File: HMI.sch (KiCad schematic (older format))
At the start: 34 parts, among them J24 Display, J25 SPI Interface, J26 I2C Interface, J27 LED3, J28 LED4, J29 Key 3, J30 Key 4, J31 Key 1, J32 Key 2, Q8 BC817, Q9 BC817, U9 74HC245

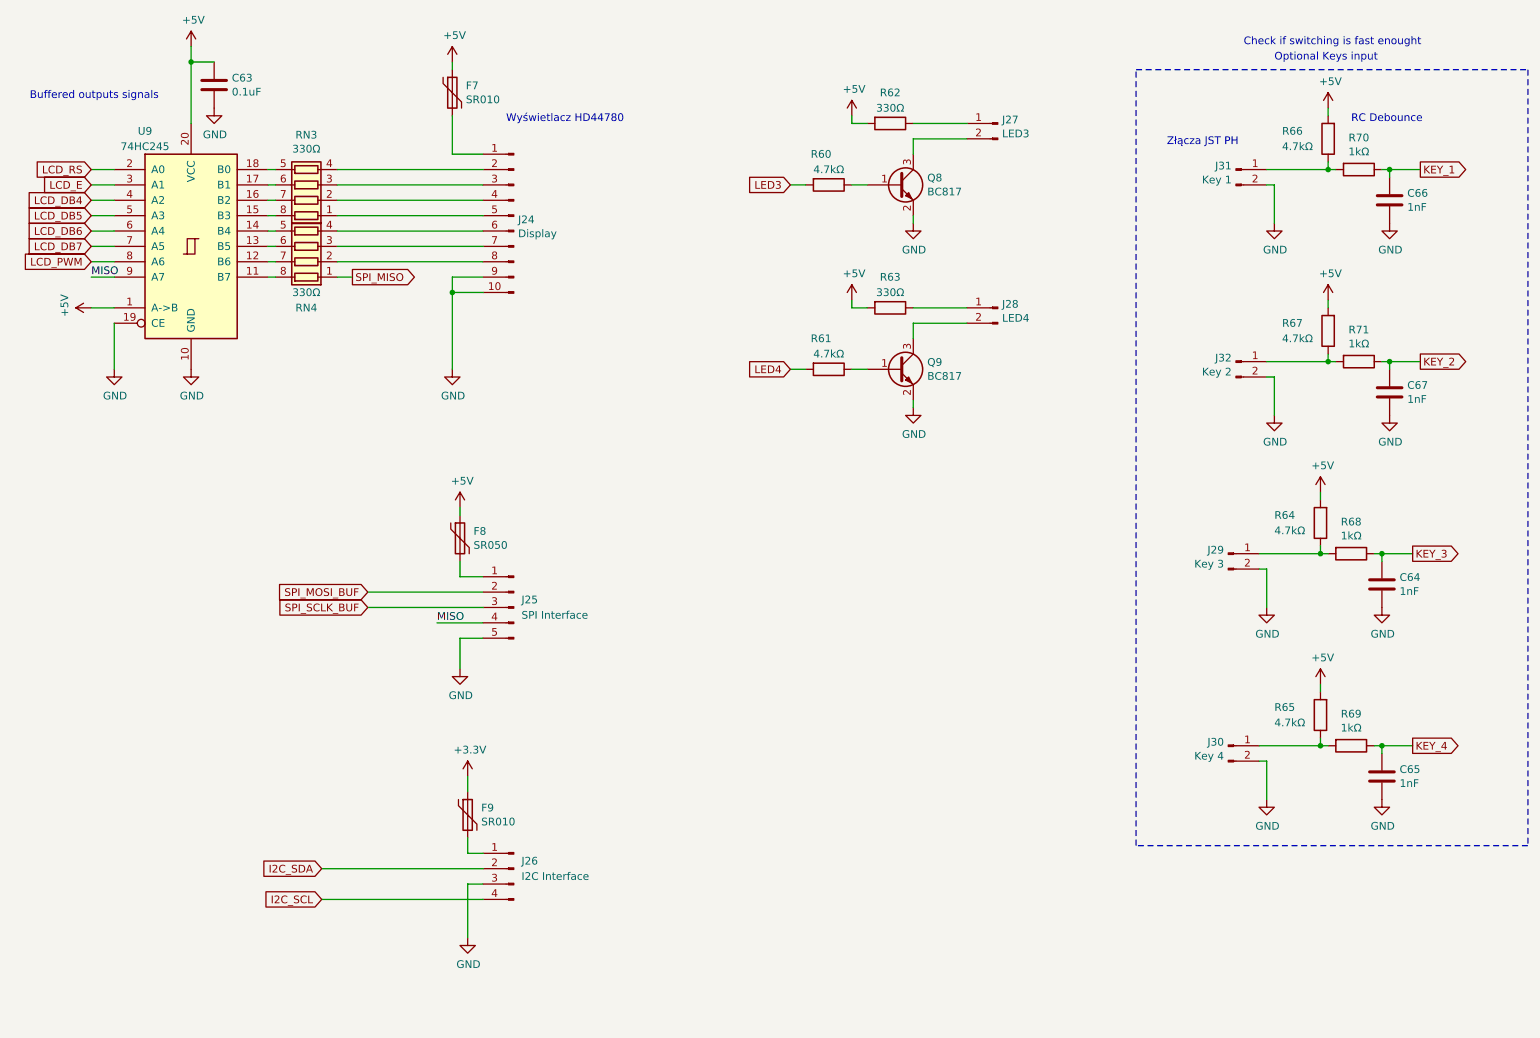
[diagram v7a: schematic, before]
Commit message: Improve Emergency, Added TVS diodes
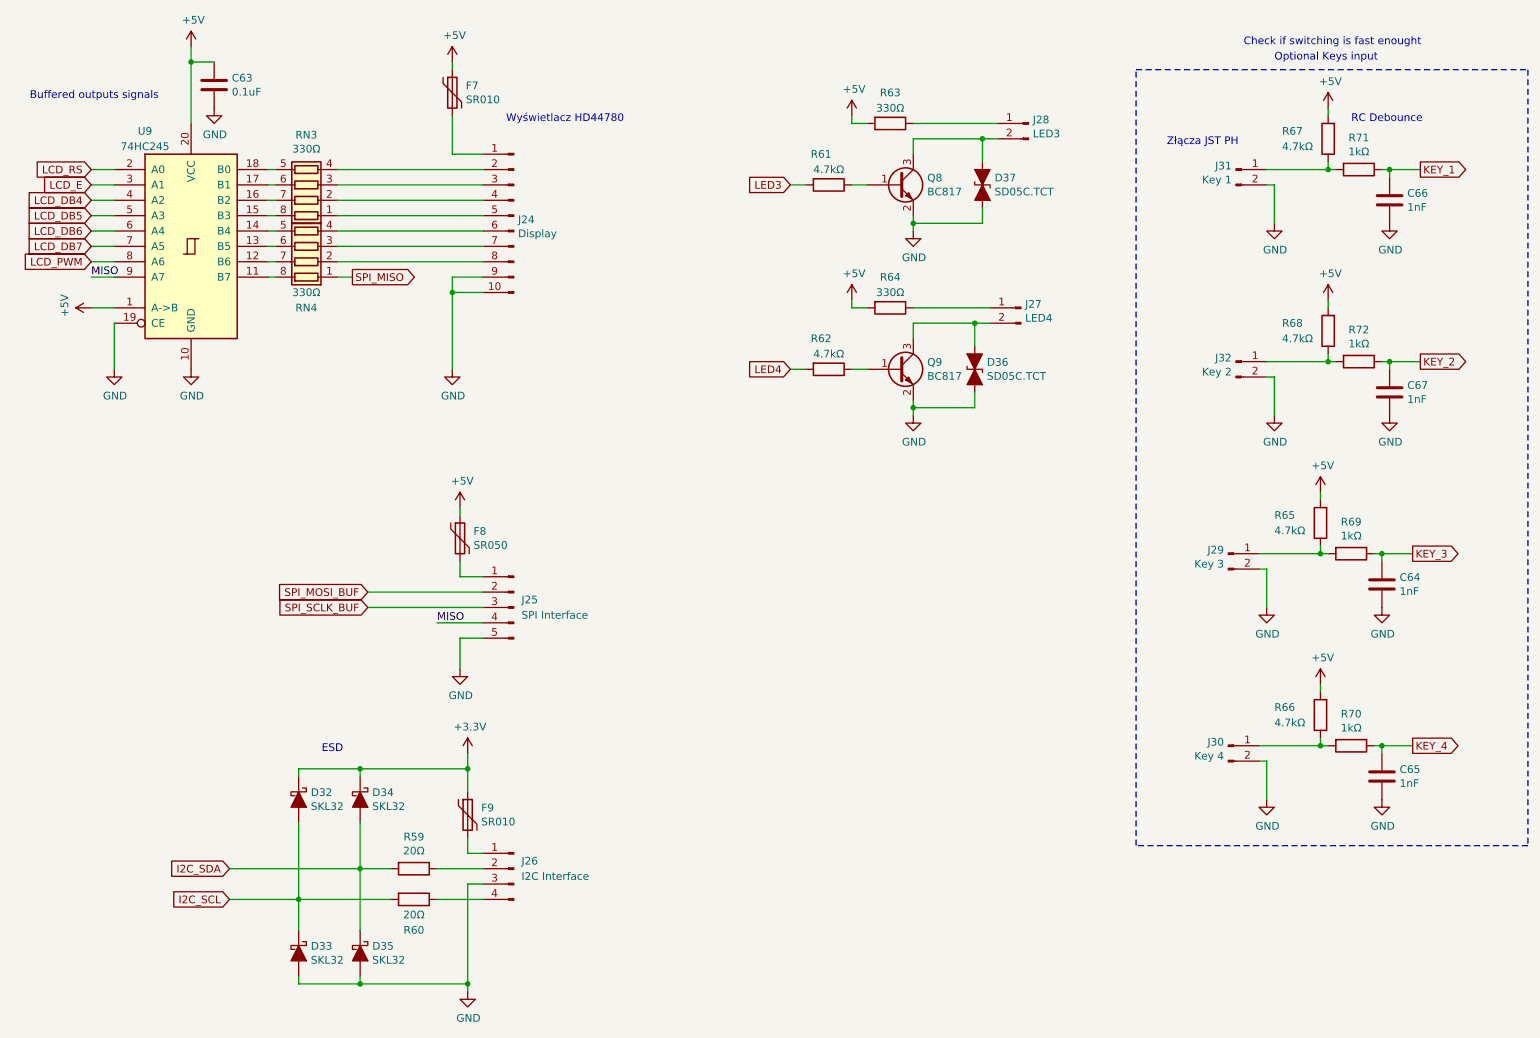
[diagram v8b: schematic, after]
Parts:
- added D32, D33, D34, D35: SKL32, Diode_SMD:D_SOD-123F, symbol Device:D_Schottky_ALT
- added D36, D37: SD05C.TCT, Diode_SMD:D_SOD-323, symbol Device:D_TVS_ALT
- added R59, R60: 20Ω, Resistor_SMD:R_0603_1608Metric, symbol Device:R
- renumbered J28 to J27, J27 to J28, R60 to R61, R61 to R62, R62 to R63, R63 to R64, R64 to R65, R65 to R66, R66 to R67, R67 to R68, R68 to R69, R69 to R70, R70 to R71, R71 to R72
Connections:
- net +3V3: now also D32.1 (K), D34.1 (K)
- net GND: now also D33.2 (A), D35.2 (A), D36.2 (A2), D37.2 (A2)
- net I2C_SCL: now also D32.2 (A), D33.1 (K), R60.2; no longer J26.4 (Pin_4)
- net I2C_SDA: now also D34.2 (A), D35.1 (K), R59.2; no longer J26.2 (Pin_2)
- net at J28.2 (Pin_2), Q8.3 (C): now also D37.1 (A1)
- net at J27.2 (Pin_2), Q9.3 (C): now also D36.1 (A1)
- new net: J26.2 (Pin_2), R59.1
- new net: J26.4 (Pin_4), R60.1
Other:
- note added: "ESD"
- moved on the sheet: J27, J28
